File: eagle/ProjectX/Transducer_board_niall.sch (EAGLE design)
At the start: 104 parts, among them T1 MA40S4S, T10 MA40S4S, T100 MA40S4S, T11 MA40S4S, T12 MA40S4S, T13 MA40S4S, T14 MA40S4S, T15 MA40S4S, T16 MA40S4S, T17 MA40S4S, T18 MA40S4S, T19 MA40S4S, T2 MA40S4S, T20 MA40S4S, T21 MA40S4S, T22 MA40S4S, T23 MA40S4S, T24 MA40S4S, T25 MA40S4S, T26 MA40S4S, T27 MA40S4S, T28 MA40S4S, T29 MA40S4S, T3 MA40S4S, T30 MA40S4S, T31 MA40S4S, T32 MA40S4S, T33 MA40S4S, T34 MA40S4S, T35 MA40S4S, T36 MA40S4S, T37 MA40S4S, T38 MA40S4S, T39 MA40S4S, T4 MA40S4S, T40 MA40S4S, T41 MA40S4S, T42 MA40S4S, T43 MA40S4S, T44 MA40S4S, T45 MA40S4S, T46 MA40S4S, T47 MA40S4S, T48 MA40S4S, T49 MA40S4S, T5 MA40S4S, T50 MA40S4S, T51 MA40S4S, T52 MA40S4S, T53 MA40S4S, T54 MA40S4S, T55 MA40S4S, T56 MA40S4S, T57 MA40S4S, T58 MA40S4S, T59 MA40S4S, T6 MA40S4S, T60 MA40S4S, T61 MA40S4S, T62 MA40S4S, T63 MA40S4S, T64 MA40S4S, T65 MA40S4S, T66 MA40S4S, T67 MA40S4S, T68 MA40S4S, T69 MA40S4S, T7 MA40S4S, T70 MA40S4S, T71 MA40S4S, T72 MA40S4S, T73 MA40S4S, T74 MA40S4S, T75 MA40S4S, T76 MA40S4S, T77 MA40S4S, T78 MA40S4S, T79 MA40S4S, T8 MA40S4S, T80 MA40S4S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

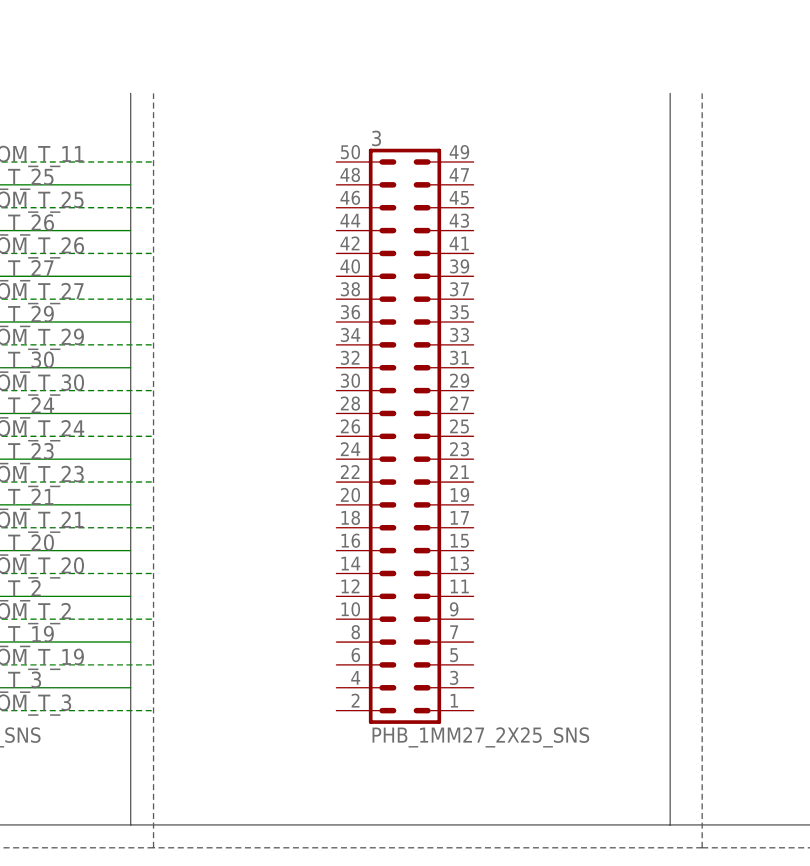
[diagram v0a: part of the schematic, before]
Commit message: Transducer board small changes
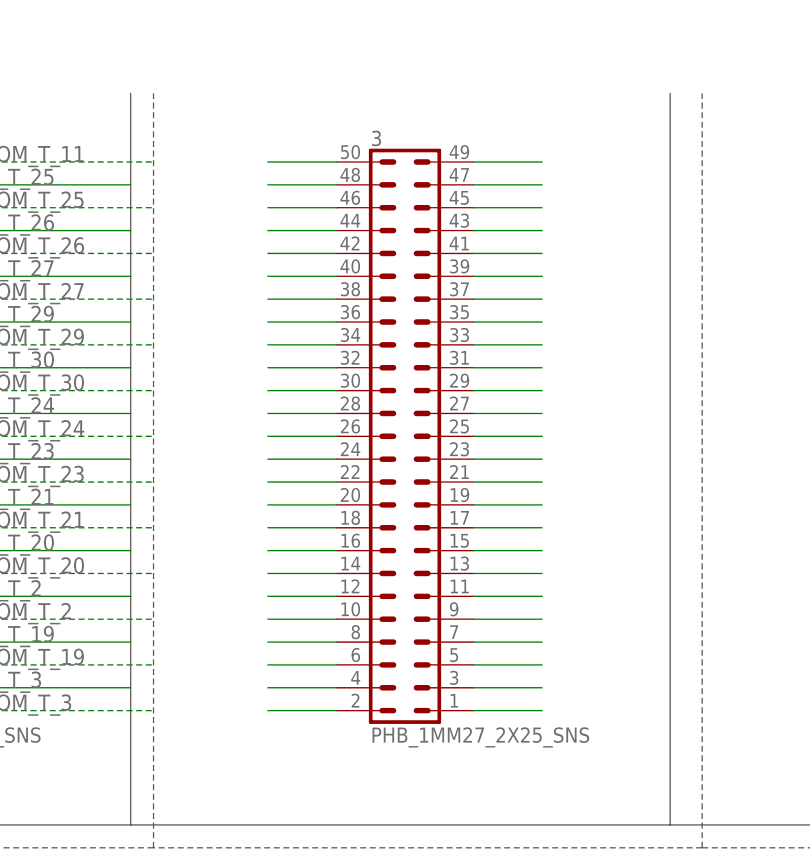
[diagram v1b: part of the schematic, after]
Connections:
- new net TEMP10: 3.34
- new net TEMP11: 3.32
- new net TEMP12: 3.30
- new net TEMP13: 3.28
- new net TEMP14: 3.26
- new net TEMP15: 3.24
- new net TEMP16: 3.22
- new net TEMP17: 3.20
- new net TEMP18: 3.18
- new net TEMP19: 3.16
- new net TEMP2: 3.50
- new net TEMP20: 3.14
- new net TEMP21: 3.12
- new net TEMP22: 3.8
- new net TEMP23: 3.6
- new net TEMP24: 3.4
- new net TEMP25: 3.2
- new net TEMP26: 3.10
- new net TEMP27: 3.1
- new net TEMP28: 3.3
- new net TEMP29: 3.5
- new net TEMP3: 3.48
- new net TEMP30: 3.7
- new net TEMP31: 3.9
- new net TEMP32: 3.11
- new net TEMP33: 3.13
- new net TEMP34: 3.15
- new net TEMP35: 3.17
- new net TEMP36: 3.19
- new net TEMP37: 3.21
- new net TEMP38: 3.23
- new net TEMP39: 3.25
- new net TEMP4: 3.46
- new net TEMP40: 3.27
- new net TEMP41: 3.29
- new net TEMP42: 3.31
- new net TEMP43: 3.33
- new net TEMP44: 3.35
- new net TEMP45: 3.37
- new net TEMP46: 3.39
- new net TEMP47: 3.41
- new net TEMP48: 3.43
- new net TEMP49: 3.45
- new net TEMP5: 3.44
- new net TEMP50: 3.47
- new net TEMP51: 3.49
- new net TEMP6: 3.42
- new net TEMP7: 3.40
- new net TEMP8: 3.38
- new net TEMP9: 3.36

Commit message: Niall almost done
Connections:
- new net TEMP100: 2.47
- new net TEMP101: 2.49
- new net TEMP52: 2.50
- new net TEMP53: 2.48
- new net TEMP54: 2.46
- new net TEMP55: 2.44
- new net TEMP56: 2.42
- new net TEMP57: 2.40
- new net TEMP58: 2.38
- new net TEMP59: 2.36
- new net TEMP60: 2.34
- new net TEMP61: 2.32
- new net TEMP62: 2.30
- new net TEMP63: 2.28
- new net TEMP64: 2.26
- new net TEMP65: 2.24
- new net TEMP66: 2.22
- new net TEMP67: 2.20
- new net TEMP68: 2.18
- new net TEMP69: 2.16
- new net TEMP70: 2.14
- new net TEMP71: 2.12
- new net TEMP72: 2.10
- new net TEMP73: 2.8
- new net TEMP74: 2.6
- new net TEMP75: 2.4
- new net TEMP76: 2.2
- new net TEMP77: 2.1
- new net TEMP78: 2.3
- new net TEMP79: 2.5
- new net TEMP80: 2.7
- new net TEMP81: 2.9
- new net TEMP82: 2.11
- new net TEMP83: 2.13
- new net TEMP84: 2.15
- new net TEMP85: 2.17
- new net TEMP86: 2.19
- new net TEMP87: 2.21
- new net TEMP88: 2.23
- new net TEMP89: 2.25
- new net TEMP90: 2.27
- new net TEMP91: 2.29
- new net TEMP92: 2.31
- new net TEMP93: 2.33
- new net TEMP94: 2.35
- new net TEMP95: 2.37
- new net TEMP96: 2.39
- new net TEMP97: 2.41
- new net TEMP98: 2.43
- new net TEMP99: 2.45

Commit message: Transducer board in finished state
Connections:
- removed net TEMP10: 3.34
- removed net TEMP100: 2.47
- removed net TEMP101: 2.49
- removed net TEMP11: 3.32
- removed net TEMP12: 3.30
- removed net TEMP13: 3.28
- removed net TEMP14: 3.26
- removed net TEMP15: 3.24
- removed net TEMP16: 3.22
- removed net TEMP17: 3.20
- removed net TEMP18: 3.18
- removed net TEMP19: 3.16
- removed net TEMP2: 3.50
- removed net TEMP20: 3.14
- removed net TEMP21: 3.12
- removed net TEMP22: 3.8
- removed net TEMP23: 3.6
- removed net TEMP24: 3.4
- removed net TEMP25: 3.2
- removed net TEMP26: 3.10
- removed net TEMP27: 3.1
- removed net TEMP28: 3.3
- removed net TEMP29: 3.5
- removed net TEMP3: 3.48
- removed net TEMP30: 3.7
- removed net TEMP31: 3.9
- removed net TEMP32: 3.11
- removed net TEMP33: 3.13
- removed net TEMP34: 3.15
- removed net TEMP35: 3.17
- removed net TEMP36: 3.19
- removed net TEMP37: 3.21
- removed net TEMP38: 3.23
- removed net TEMP39: 3.25
- removed net TEMP4: 3.46
- removed net TEMP40: 3.27
- removed net TEMP41: 3.29
- removed net TEMP42: 3.31
- removed net TEMP43: 3.33
- removed net TEMP44: 3.35
- removed net TEMP45: 3.37
- removed net TEMP46: 3.39
- removed net TEMP47: 3.41
- removed net TEMP48: 3.43
- removed net TEMP49: 3.45
- removed net TEMP5: 3.44
- removed net TEMP50: 3.47
- removed net TEMP51: 3.49
- removed net TEMP52: 2.50
- removed net TEMP53: 2.48
- removed net TEMP54: 2.46
- removed net TEMP55: 2.44
- removed net TEMP56: 2.42
- removed net TEMP57: 2.40
- removed net TEMP58: 2.38
- removed net TEMP59: 2.36
- removed net TEMP6: 3.42
- removed net TEMP60: 2.34
- removed net TEMP61: 2.32
- removed net TEMP62: 2.30
- removed net TEMP63: 2.28
- removed net TEMP64: 2.26
- removed net TEMP65: 2.24
- removed net TEMP66: 2.22
- removed net TEMP67: 2.20
- removed net TEMP68: 2.18
- removed net TEMP69: 2.16
- removed net TEMP7: 3.40
- removed net TEMP70: 2.14
- removed net TEMP71: 2.12
- removed net TEMP72: 2.10
- removed net TEMP73: 2.8
- removed net TEMP74: 2.6
- removed net TEMP75: 2.4
- removed net TEMP76: 2.2
- removed net TEMP77: 2.1
- removed net TEMP78: 2.3
- removed net TEMP79: 2.5
- removed net TEMP8: 3.38
- removed net TEMP80: 2.7
- removed net TEMP81: 2.9
- removed net TEMP82: 2.11
- removed net TEMP83: 2.13
- removed net TEMP84: 2.15
- removed net TEMP85: 2.17
- removed net TEMP86: 2.19
- removed net TEMP87: 2.21
- removed net TEMP88: 2.23
- removed net TEMP89: 2.25
- removed net TEMP9: 3.36
- removed net TEMP90: 2.27
- removed net TEMP91: 2.29
- removed net TEMP92: 2.31
- removed net TEMP93: 2.33
- removed net TEMP94: 2.35
- removed net TEMP95: 2.37
- removed net TEMP96: 2.39
- removed net TEMP97: 2.41
- removed net TEMP98: 2.43
- removed net TEMP99: 2.45
- net FROM_T_31: now also 3.48
- net FROM_T_32: now also 3.44
- net FROM_T_33: now also 3.36
- net FROM_T_34: now also 3.32
- net FROM_T_35: now also 3.20
- net FROM_T_36: now also 3.16
- net FROM_T_37: now also 3.12
- net FROM_T_38: now also 3.8
- net FROM_T_39: now also 3.4
- net FROM_T_40: now also 3.5
- net FROM_T_41: now also 3.9
- net FROM_T_42: now also 3.1
- net FROM_T_43: now also 3.24
- net FROM_T_44: now also 3.28
- net FROM_T_47: now also 3.40
- net FROM_T_48: now also 3.49
- net FROM_T_53: now also 3.45
- net FROM_T_54: now also 3.41
- net FROM_T_57: now also 3.21
- net FROM_T_58: now also 3.17
- net FROM_T_59: now also 3.13
- net FROM_T_61: now also 2.8
- net FROM_T_62: now also 2.12
- net FROM_T_63: now also 2.16
- net FROM_T_64: now also 2.20
- net FROM_T_65: now also 3.25
- net FROM_T_66: now also 3.29
- net FROM_T_67: now also 3.33
- net FROM_T_68: now also 3.37
- net FROM_T_73: now also 2.44
- net FROM_T_74: now also 2.40
- net FROM_T_75: now also 2.36
- net FROM_T_76: now also 2.32
- net FROM_T_77: now also 2.28
- net FROM_T_78: now also 2.24
- net FROM_T_80: now also 2.4
- net FROM_T_81: now also 2.1
- net FROM_T_82: now also 2.9
- net FROM_T_83: now also 2.25
- net FROM_T_84: now also 2.21
- net FROM_T_85: now also 2.29
- net FROM_T_86: now also 2.37
- net FROM_T_87: now also 2.45
- net FROM_T_88: now also 2.48
- net FROM_T_93: now also 2.49
- net FROM_T_94: now also 2.41
- net FROM_T_95: now also 2.33
- net FROM_T_97: now also 2.17
- net FROM_T_98: now also 2.13
- net FROM_T_99: now also 2.5
- net TO_T_31: now also 3.46
- net TO_T_32: now also 3.42
- net TO_T_33: now also 3.34
- net TO_T_34: now also 3.30
- net TO_T_35: now also 3.18
- net TO_T_36: now also 3.14
- net TO_T_37: now also 3.10
- net TO_T_38: now also 3.6
- net TO_T_39: now also 3.2
- net TO_T_40: now also 3.7
- net TO_T_41: now also 3.11
- net TO_T_42: now also 3.3
- net TO_T_43: now also 3.22
- net TO_T_44: now also 3.26
- net TO_T_47: now also 3.38
- net TO_T_48: now also 3.50
- net TO_T_53: now also 3.47
- net TO_T_54: now also 3.43
- net TO_T_57: now also 3.23
- net TO_T_58: now also 3.19
- net TO_T_59: now also 3.15
- net TO_T_61: now also 2.6
- net TO_T_62: now also 2.10
- net TO_T_63: now also 2.14
- net TO_T_64: now also 2.18
- net TO_T_65: now also 3.27
- net TO_T_66: now also 3.31
- net TO_T_67: now also 3.35
- net TO_T_68: now also 3.39
- net TO_T_73: now also 2.42
- net TO_T_74: now also 2.38
- net TO_T_75: now also 2.34
- net TO_T_76: now also 2.30
- net TO_T_77: now also 2.26
- net TO_T_78: now also 2.22
- net TO_T_80: now also 2.2
- net TO_T_81: now also 2.3
- net TO_T_82: now also 2.11
- net TO_T_83: now also 2.27
- net TO_T_84: now also 2.23
- net TO_T_85: now also 2.31
- net TO_T_86: now also 2.39
- net TO_T_87: now also 2.47
- net TO_T_88: now also 2.46
- net TO_T_93: now also 2.50
- net TO_T_94: now also 2.43
- net TO_T_95: now also 2.35
- net TO_T_97: now also 2.19
- net TO_T_98: now also 2.15
- net TO_T_99: now also 2.7

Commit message: Transducer board in finished state
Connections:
- removed net FROM_T_11: 4.49, T11.1
- new net SHIELD: 4.49
- net FROM_T_12: now also T11.1
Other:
- note added: "connected 11 and 12 grounds together"
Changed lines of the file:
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@@
 <rectangle x1="-95.25" y1="241.554" x2="-73.66" y2="256.54" layer="91"/>
 <text x="-161.29" y="248.412" size="1.778" layer="91">Transievers Green</text>
+<text x="-26.162" y="288.036" size="1.778" layer="91">connected 11 and 12 grounds together</text>
 </plain>
 <instances>
@@
 </segment>
 </net>
-<net name="FROM_T_11" class="0">
+<net name="TO_T_11" class="0">
+<segment>
+<wire x1="-7.62" y1="271.78" x2="-7.62" y2="279.4" width="0.1524" layer="91"/>
+<label x="-7.62" y="274.32" size="1.778" layer="95"/>
+<pinref part="T11" gate="G$1" pin="2"/>
+</segment>
+<segment>
+<pinref part="4" gate="G$1" pin="50"/>
+<wire x1="-210.82" y1="185.42" x2="-231.14" y2="185.42" width="0.1524" layer="91"/>
+<label x="-226.06" y="185.42" size="1.778" layer="95"/>
+</segment>
+</net>
+<net name="FROM_T_12" class="0">
+<segment>
+<wire x1="5.08" y1="287.02" x2="5.08" y2="279.4" width="0.1524" layer="91"/>
+<label x="4.572" y="286.004" size="1.778" layer="95" rot="R180"/>
+<pinref part="T12" gate="G$1" pin="1"/>
+</segment>
+<segment>
+<pinref part="4" gate="G$1" pin="48"/>
+<wire x1="-210.82" y1="182.88" x2="-228.6" y2="182.88" width="0.1524" layer="91" style="dashdot"/>
+<label x="-226.06" y="182.88" size="1.778" layer="95"/>
+</segment>
 <segment>
 <wire x1="-17.78" y1="287.02" x2="-17.78" y2="279.4" width="0.1524" layer="91"/>
@@
 <pinref part="T11" gate="G$1" pin="1"/>
 </segment>
-<segment>
-<pinref part="4" gate="G$1" pin="49"/>
-<wire x1="-195.58" y1="185.42" x2="-170.18" y2="185.42" width="0.1524" layer="91" style="dashdot"/>
-<label x="-190.5" y="185.42" size="1.778" layer="95"/>
-</segment>
-</net>
-<net name="TO_T_11" class="0">
-<segment>
-<wire x1="-7.62" y1="271.78" x2="-7.62" y2="279.4" width="0.1524" layer="91"/>
-<label x="-7.62" y="274.32" size="1.778" layer="95"/>
-<pinref part="T11" gate="G$1" pin="2"/>
-</segment>
-<segment>
-<pinref part="4" gate="G$1" pin="50"/>
-<wire x1="-210.82" y1="185.42" x2="-231.14" y2="185.42" width="0.1524" layer="91"/>
-<label x="-226.06" y="185.42" size="1.778" layer="95"/>
-</segment>
-</net>
-<net name="FROM_T_12" class="0">
-<segment>
-<wire x1="5.08" y1="287.02" x2="5.08" y2="279.4" width="0.1524" layer="91"/>
-<label x="4.572" y="286.004" size="1.778" layer="95" rot="R180"/>
-<pinref part="T12" gate="G$1" pin="1"/>
-</segment>
-<segment>
-<pinref part="4" gate="G$1" pin="48"/>
-<wire x1="-210.82" y1="182.88" x2="-228.6" y2="182.88" width="0.1524" layer="91" style="dashdot"/>
-<label x="-226.06" y="182.88" size="1.778" layer="95"/>
-</segment>
 </net>
 <net name="TO_T_12" class="0">
@@
 </segment>
 </net>
+<net name="SHIELD" class="0">
+<segment>
+<pinref part="4" gate="G$1" pin="49"/>
+<wire x1="-195.58" y1="185.42" x2="-193.04" y2="185.42" width="0.1524" layer="91"/>
+<wire x1="-193.04" y1="185.42" x2="-193.04" y2="200.66" width="0.1524" layer="91"/>
+<label x="-197.104" y="200.66" size="1.778" layer="95"/>
+</segment>
+</net>

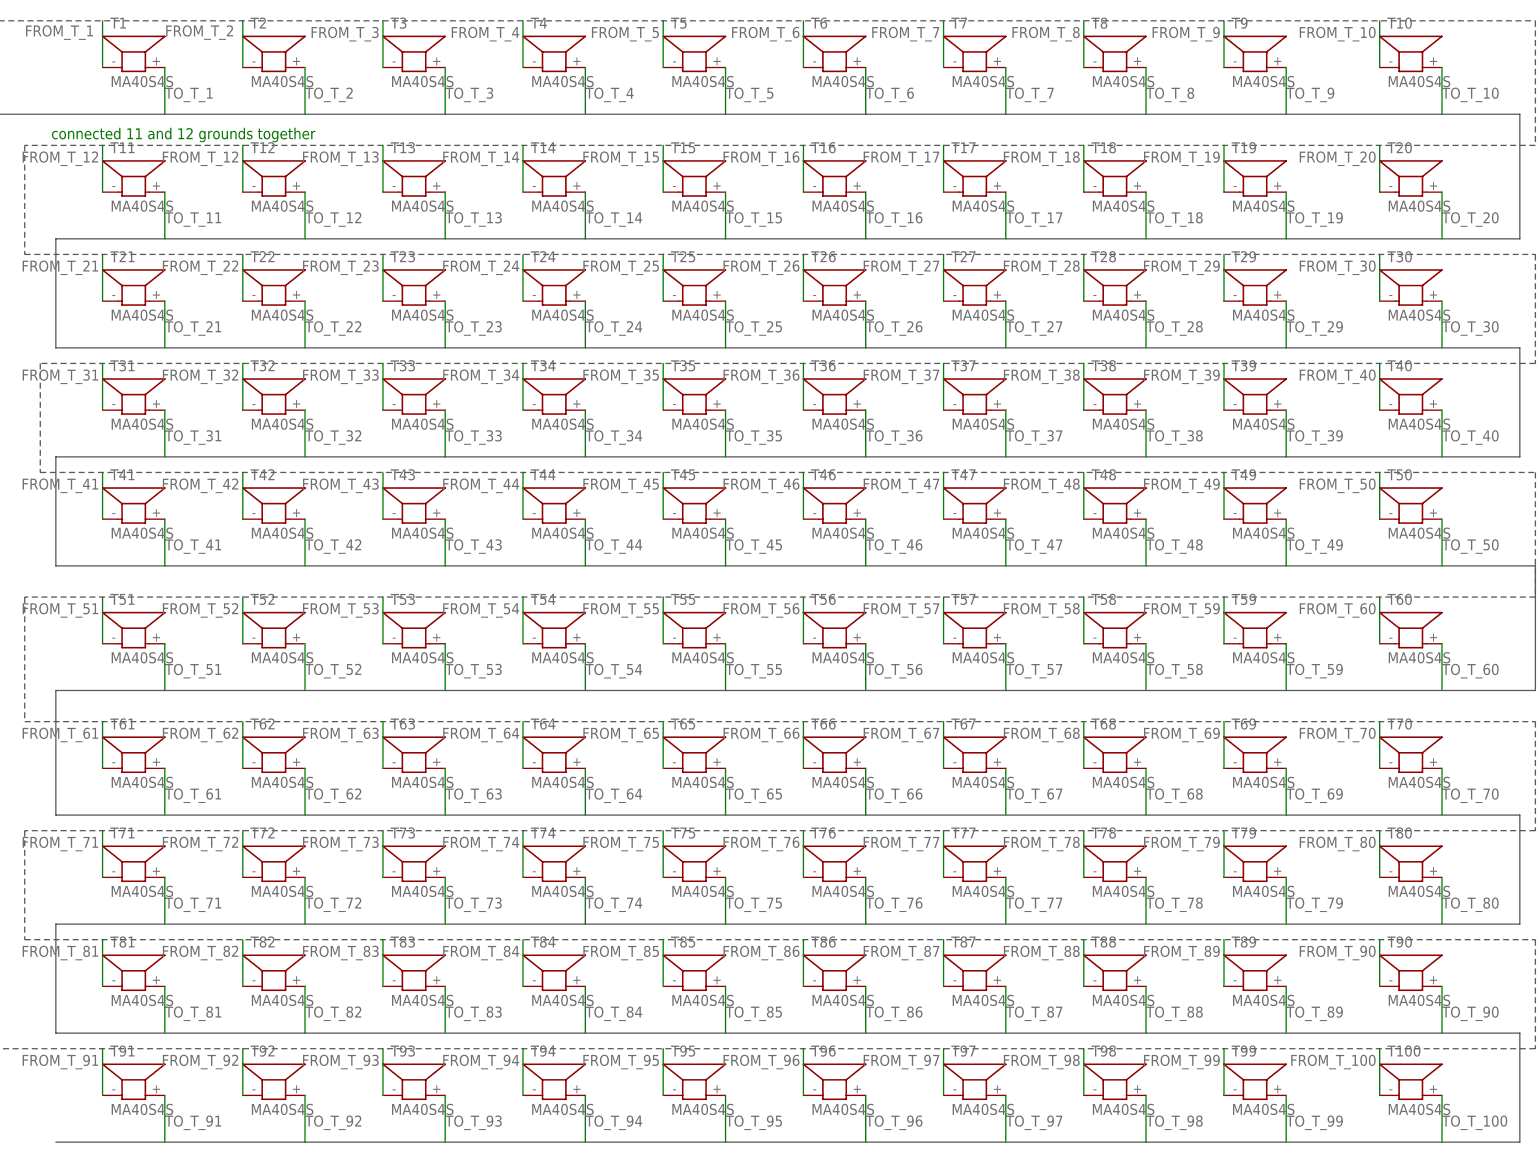
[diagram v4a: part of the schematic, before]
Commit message: New transducer numbering start
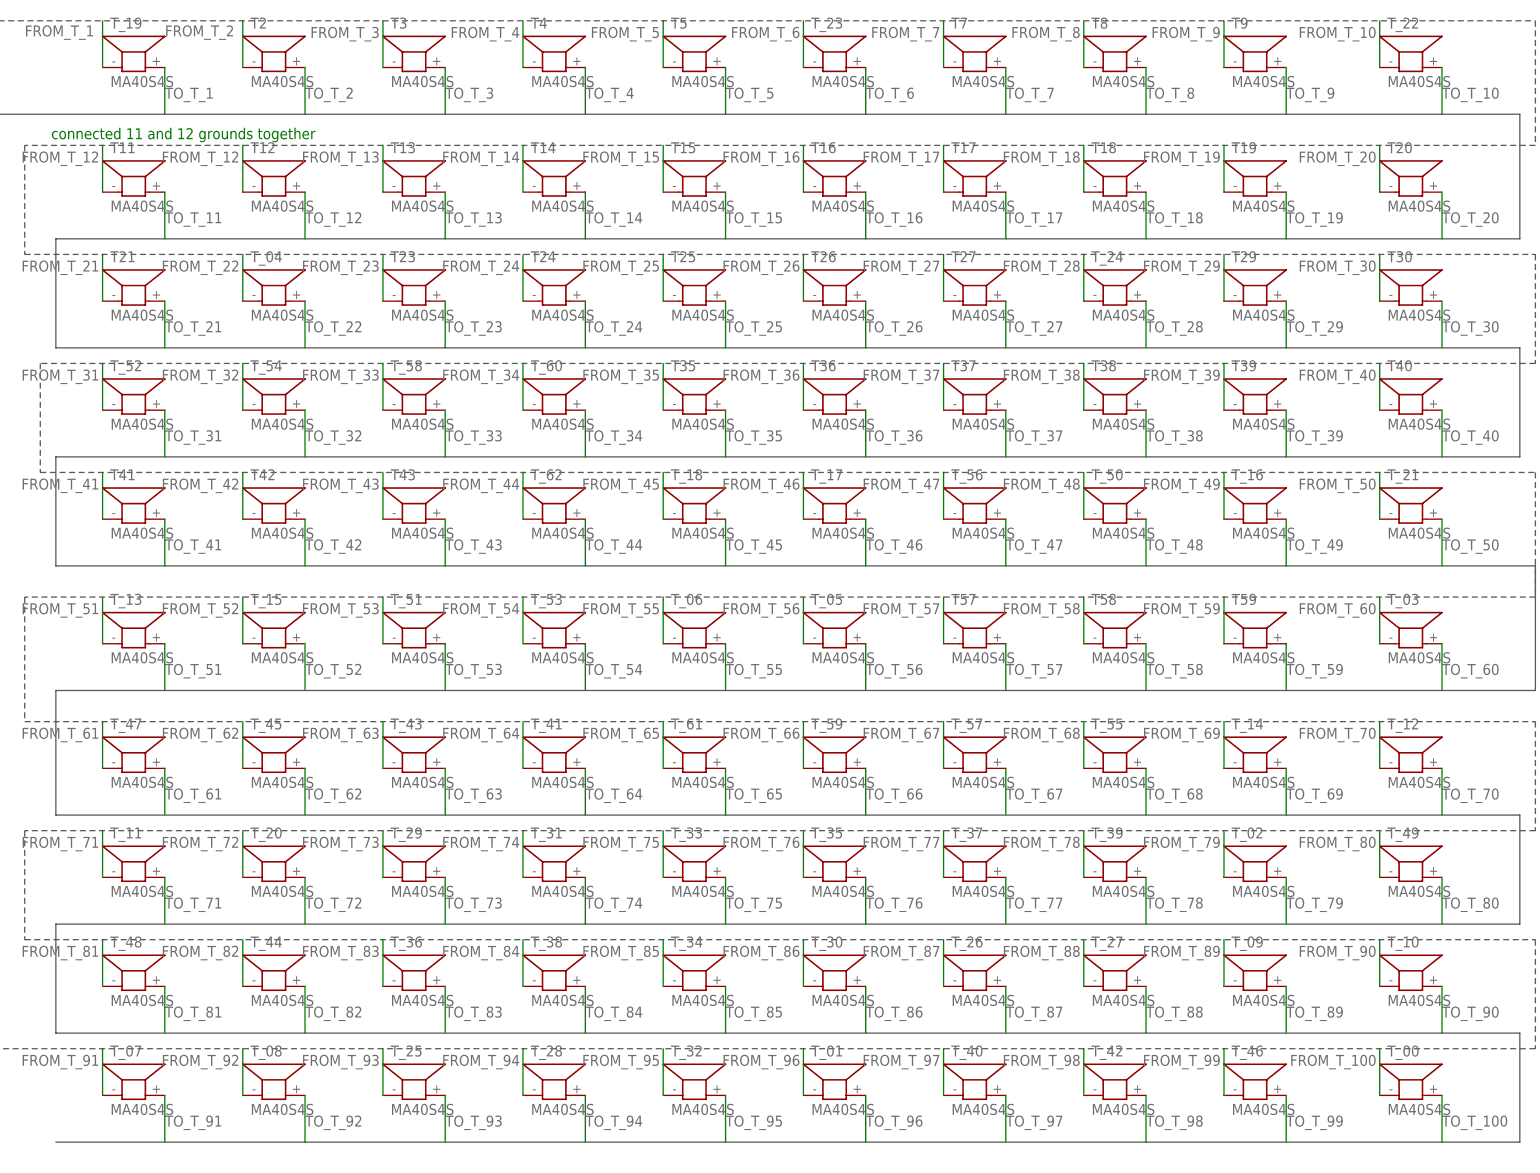
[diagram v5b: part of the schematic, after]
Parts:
- renumbered T1 to T_19, T10 to T_22, T100 to T_00, T22 to T_04, T28 to T_24, T31 to T_52, T32 to T_54, T33 to T_58, T34 to T_60, T44 to T_62, T45 to T_18, T46 to T_17, T47 to T_56, T48 to T_50, T49 to T_16, T50 to T_21, T51 to T_13, T52 to T_15, T53 to T_51, T54 to T_53, T55 to T_06, T56 to T_05, T6 to T_23, T60 to T_03, T61 to T_47, T62 to T_45, T63 to T_43, T64 to T_41, T65 to T_61, T66 to T_59, T67 to T_57, T68 to T_55, T69 to T_14, T70 to T_12, T71 to T_11, T72 to T_20, T73 to T_29, T74 to T_31, T75 to T_33, T76 to T_35, T77 to T_37, T78 to T_39, T79 to T_02, T80 to T_49, T81 to T_48, T82 to T_44, T83 to T_36, T84 to T_38, T85 to T_34, T86 to T_30, T87 to T_26, T88 to T_27, T89 to T_09, T90 to T_10, T91 to T_07, T92 to T_08, T93 to T_25, T94 to T_28, T95 to T_32, T96 to T_01, T97 to T_40, T98 to T_42, T99 to T_46

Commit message: Boards almost done
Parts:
- renumbered T11 to T_75, T12 to T_77, T13 to T_79, T14 to T_81, T15 to T_83, T16 to T_85, T17 to T_87, T18 to T_89, T19 to T_96, T2 to T_94, T20 to T_92, T21 to T_90, T23 to T_88, T24 to T_86, T25 to T_76, T26 to T_78, T27 to T_80, T29 to T_82, T3 to T_98, T30 to T_84, T35 to T_66, T36 to T_68, T37 to T_70, T38 to T_72, T39 to T_74, T4 to T_99, T40 to T_71, T41 to T_69, T42 to T_73, T43 to T_64, T5 to T_97, T57 to T_63, T58 to T_65, T59 to T_67, T7 to T_95, T8 to T_93, T9 to T_91
